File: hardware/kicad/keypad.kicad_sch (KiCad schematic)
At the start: 36 parts, among them SW1 SW_Push, SW10 SW_Push, SW11 SW_Push, SW12 SW_Push, SW13 SW_Push, SW14 SW_Push, SW15 SW_Push, SW16 SW_Push, SW17 SW_Push, SW18 SW_Push, SW19 SW_Push, SW2 SW_Push, SW20 SW_Push, SW21 SW_Push, SW22 SW_Push, SW23 SW_Push, SW24 SW_Push, SW25 SW_Push, SW26 SW_Push, SW27 SW_Push, SW28 SW_Push, SW29 SW_Push, SW3 SW_Push, SW30 SW_Push, SW31 SW_Push, SW32 SW_Push, SW33 SW_Push, SW34 SW_Push, SW35 SW_Push, SW36 SW_Push, SW4 SW_Push, SW5 SW_Push, SW6 SW_Push, SW7 SW_Push, SW8 SW_Push, SW9 SW_Push

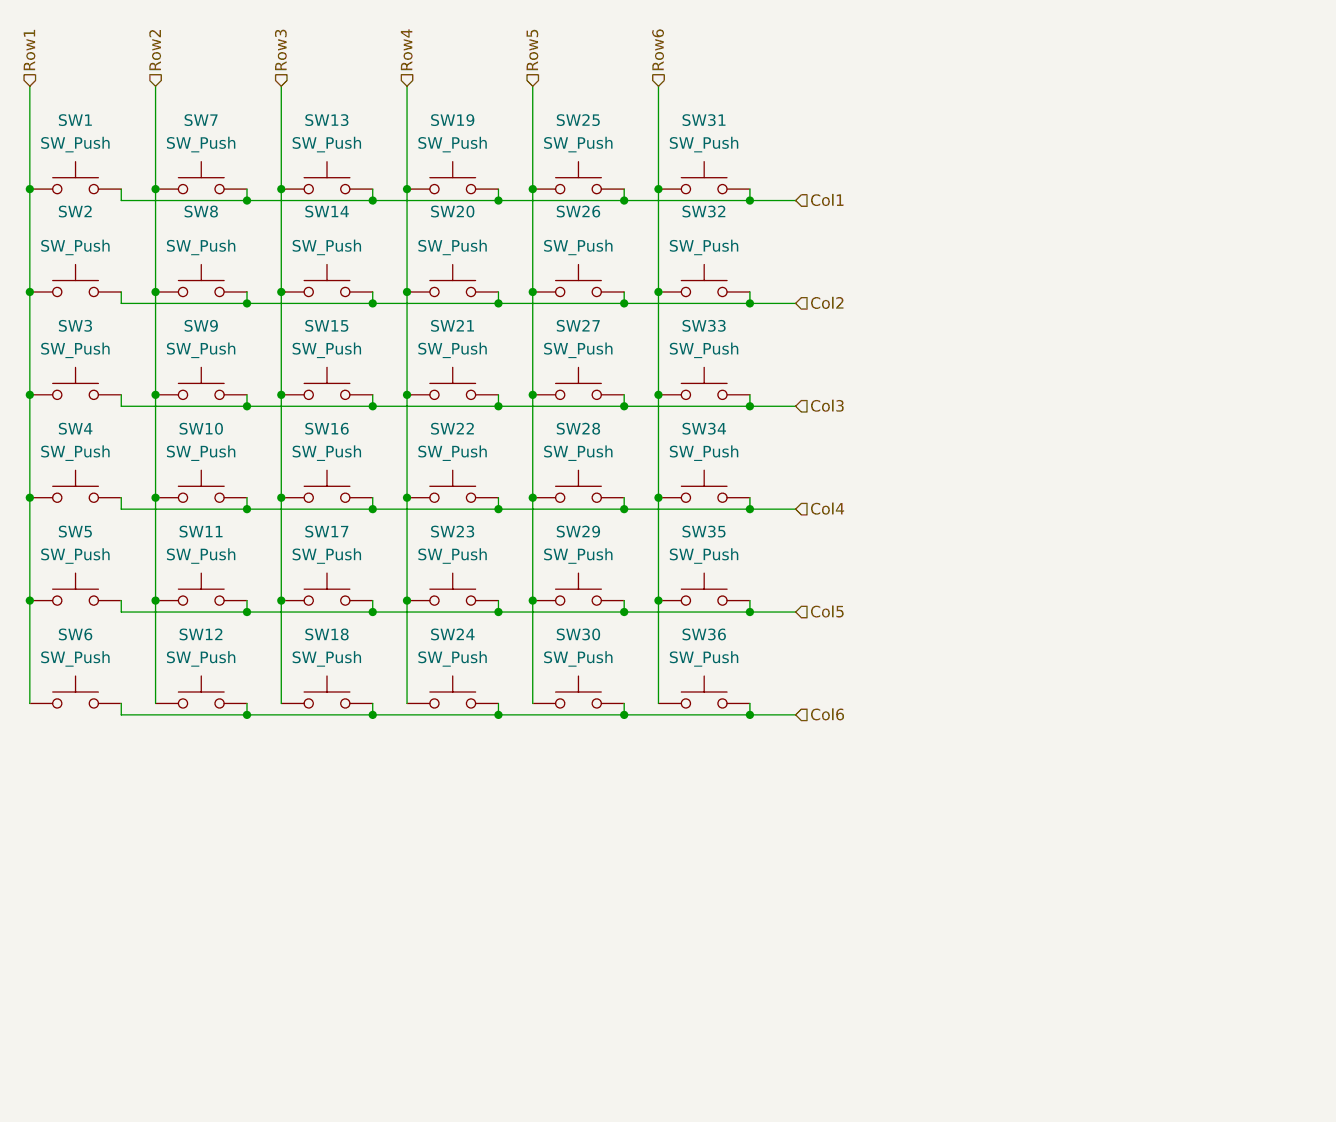
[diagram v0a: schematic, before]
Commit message: KiCad 10 & 3D 	删除：     hardware/gerber.zip 	新文件：   hardware/gerber260722.zip 	新文件：   "hardware/kicad/AZ-Delivery_18\350\213\261\345\257\270TFT\346\230\276\347\244\272\345\261\217SPI/AZ-Delivery 1.8 inch TFT Display SPI.jpg" 	新文件：   "hardware/kicad/AZ-Delivery_18\350\213\261\345\257\270TFT\346\230\276\347\244\272\345\261\217SPI/AZ-Delivery 1.8 inch TFT Display SPI.pdf" 	新文件：   "hardware/kicad/AZ-Delivery_18\350\213\261\345\257\270TFT\346\230\276\347\244\272\345\261\217SPI/AZ-Delivery 1.8 inch TFT Display SPI.stp" 	新文件：   "hardware/kicad/AZ-Delivery_18\350\213\261\345\257\270TFT\346\230\276\347\244\272\345\261\217SPI/AZ-Delivery 1.8 inch TFT Display SP_2I.jpg" 	新文件：   hardware/kicad/Arduino_Nano/Nano290313.jpg 	新文件：   hardware/kicad/Arduino_Nano/arduino nano.igs 	新文件：   hardware/kicad/Arduino_Nano/arduino nano.step 	新文件：   hardware/kicad/Arduino_Nano/arduino nano290313.zip 	新文件：   hardware/kicad/Arduino_Nano/nano top finised.jpg 	新文件：   hardware/kicad/Arduino_Nano/nano underside2.jpg 	修改：     hardware/kicad/calculator.kicad_pcb 	新文件：   hardware/kicad/calculator.kicad_prl 	修改：     hardware/kicad/calculator.kicad_pro 	新文件：   hardware/kicad/calculator_t.png 	新文件：   hardware/kicad/fp-info-cache 	新文件：   hardware/kicad/fp-lib-table 	修改：     hardware/kicad/keypad.kicad_sch 	新文件：   hardware/kicad/sym-lib-table
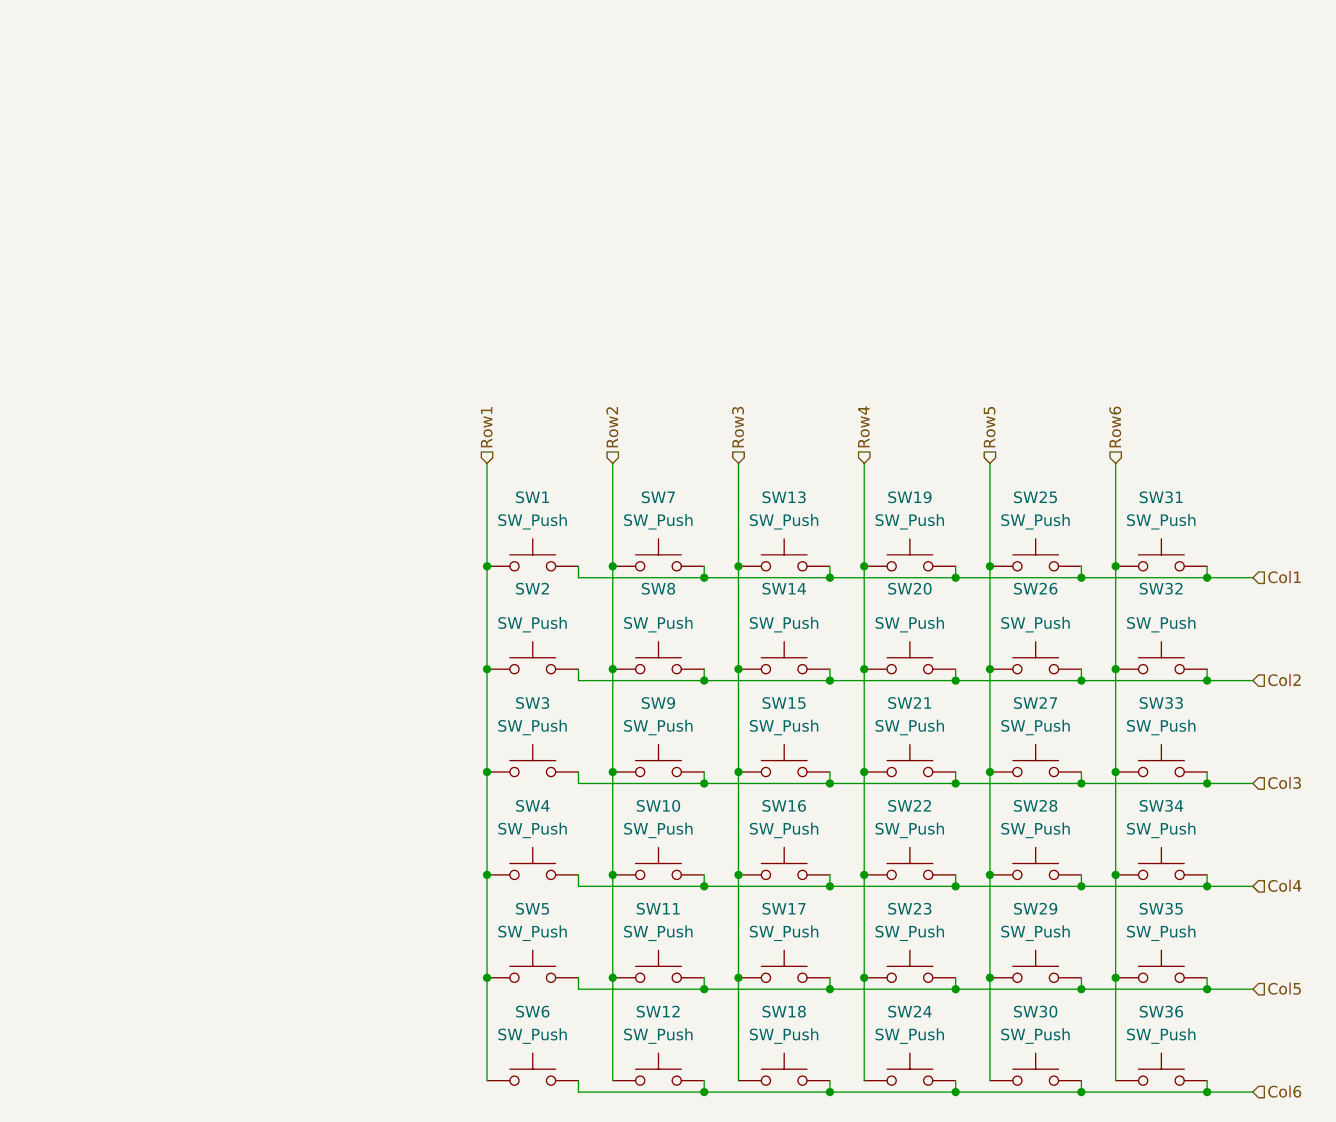
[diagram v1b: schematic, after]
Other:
- moved on the sheet: SW1, SW10, SW11, SW12, SW13, SW14, SW15, SW16, SW17, SW18, SW19, SW2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
